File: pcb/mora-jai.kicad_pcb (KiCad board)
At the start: 2 copper layers, 150 x 150 mm, 74 parts, among them J1 Conn_01x02, J2 Conn_01x04, J3 Conn_01x02, J4 Conn_01x01, J5 Conn_01x03, SW1 SW_Push, SW10 SW_Push, SW11 SW_Push, SW12 SW_Push, SW13 SW_Push, SW14 SW_Push, SW15 SW_Push, SW16 SW_Push, SW2 SW_Push, SW3 SW_Push, SW4 SW_Push, SW5 SW_Push, SW6 SW_Push, SW7 SW_Push, SW8 SW_Push, SW9 SW_Push, U1 CD74HC4067M, U3 XIAO-ESP32-S3-SMD

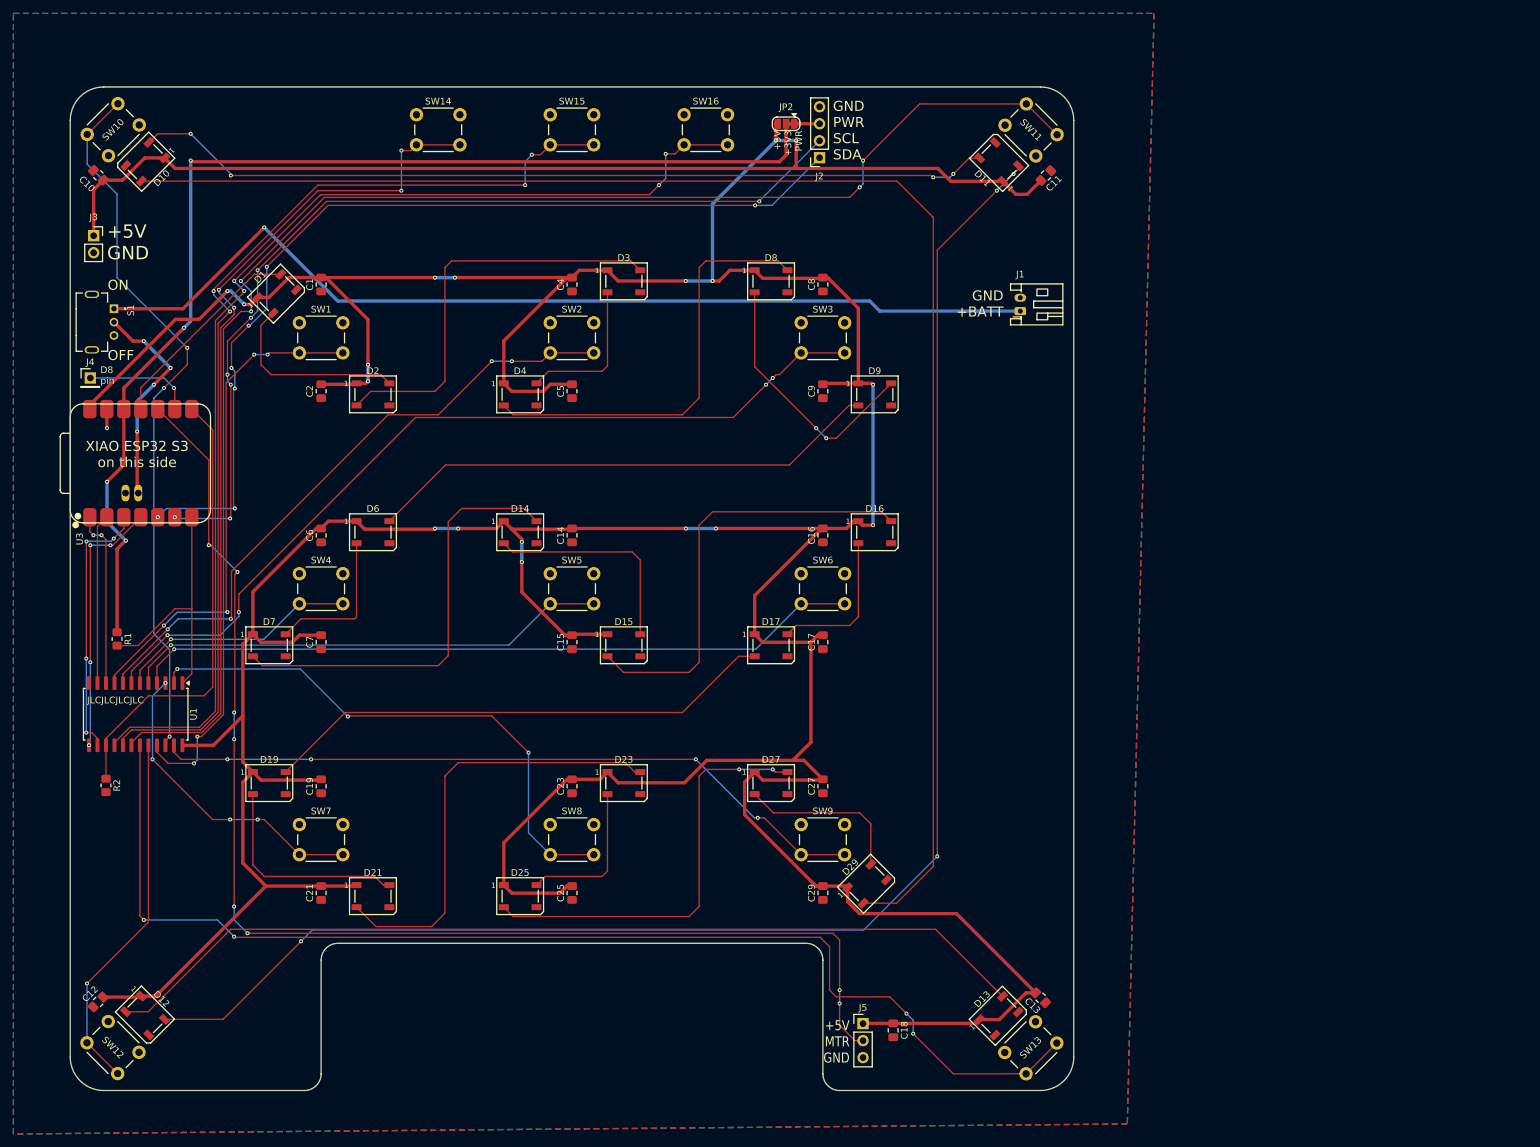
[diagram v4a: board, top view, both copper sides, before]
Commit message: add ground connecting vias
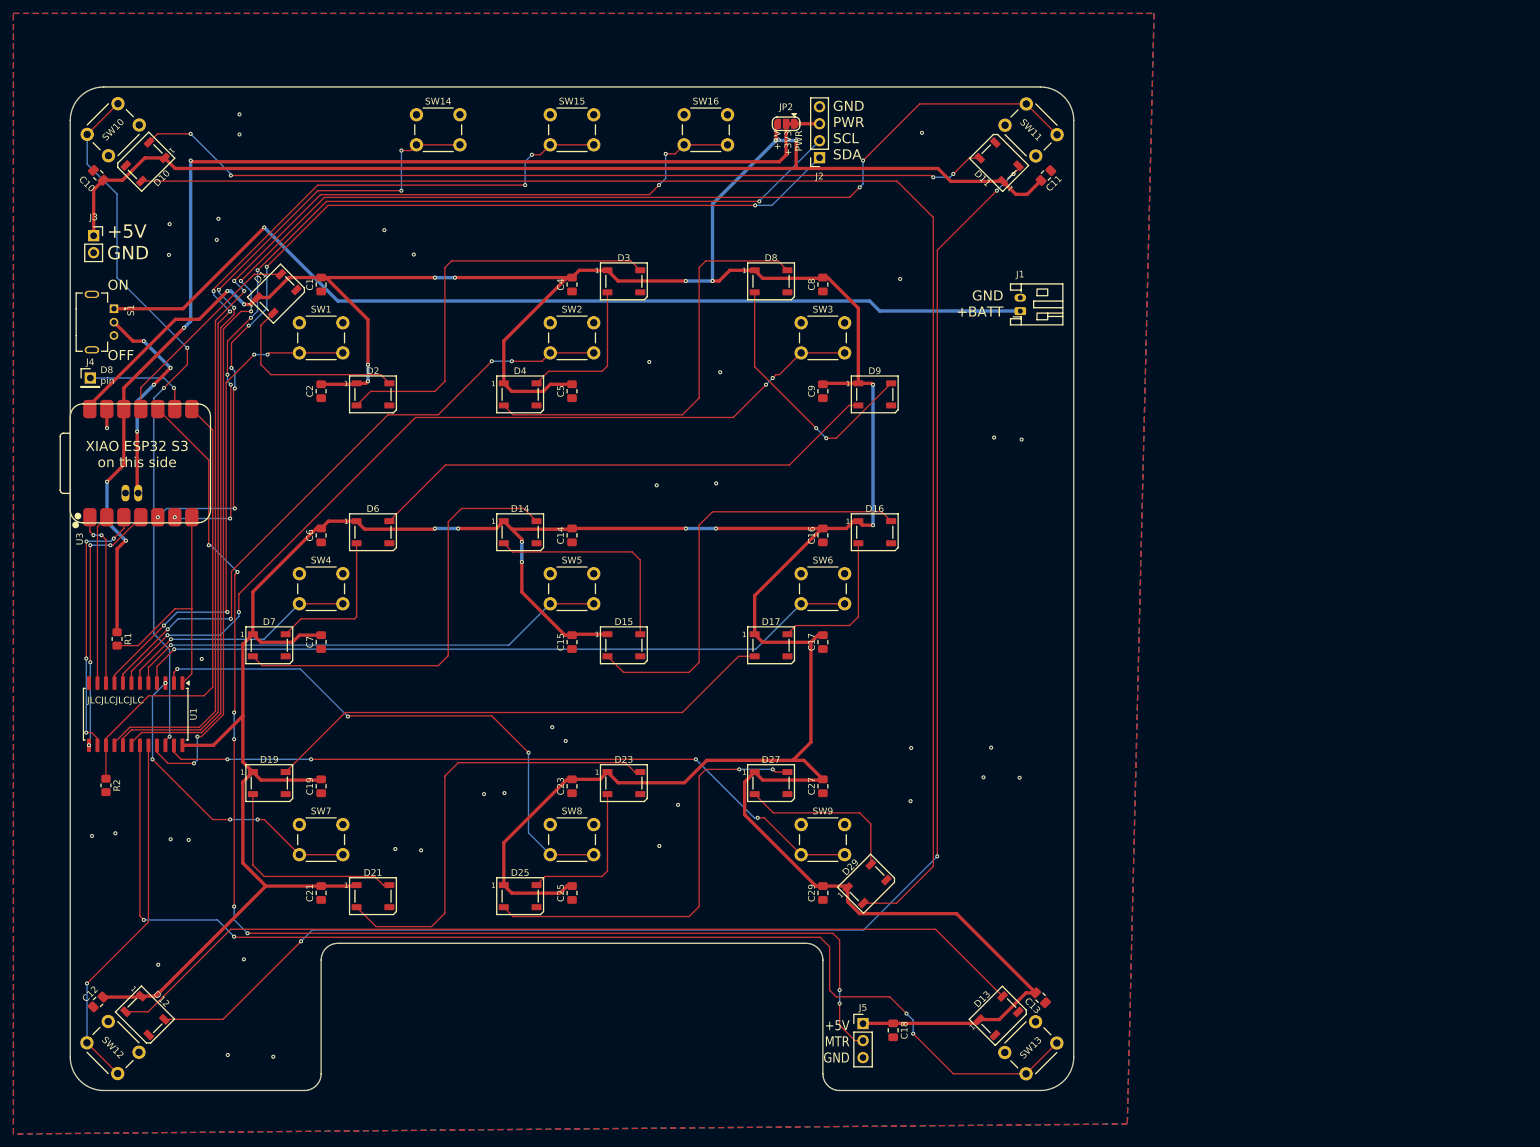
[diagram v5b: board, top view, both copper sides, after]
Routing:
- net GND: vias 1 -> 39

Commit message: add notes to PCB and schematic for revision 2
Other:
- board text added: "TODO: - Add mounting hole cutouts - Add battery charger & boost circuits (see schematic)"

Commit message: added mounting holes, 3.5mm diameter
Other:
- outline, holes or cut-outs redrawn
- board text added: "TODO: - Add battery charger & boost circuits (see schematic)"
- board text removed: "TODO: - Add mounting hole cutouts - Add battery charger & boost circuits (see schematic)"

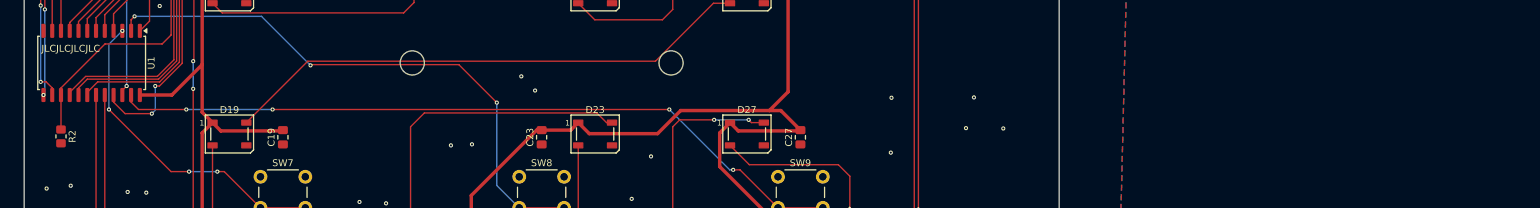
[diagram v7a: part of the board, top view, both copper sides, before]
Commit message: finished (?) schematic for rev. 2 power circuits
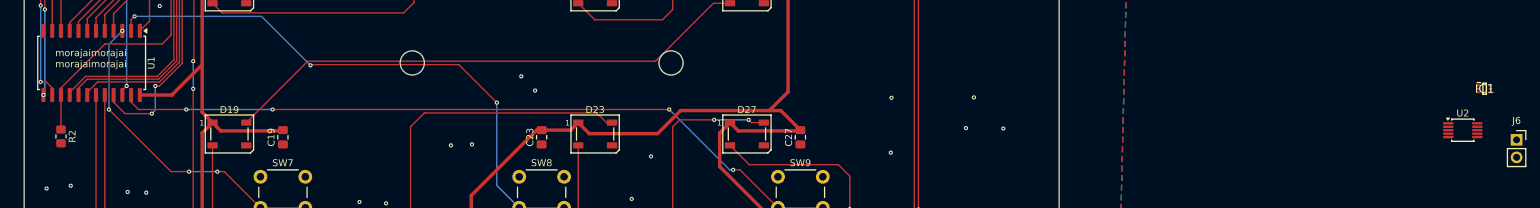
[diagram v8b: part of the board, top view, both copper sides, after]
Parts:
- added IC1: TPS61023DRLR, Mora_Jai_Parts:SOTFL50P160X60-6N, F.Cu at (237.7, 120.5)
- added J6: Conn_01x02, Connector_PinSocket_2.54mm:PinSocket_1x02_P2.54mm_Vertical, F.Cu at (242.3, 127.9)
- added U2: MCP73833-AMI-UN, Package_SO:MSOP-10_3x3mm_P0.5mm, F.Cu at (234.5, 126.5)
- R1, R2: value R -> 100kΩ
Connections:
- J1 pad 1: Net-(J1-Pin_1) -> unconnected-(J1-Pin_1-Pad1)
- R2 pad 1: /MUX_EN -> Net-(U1-~{E})
- S1 pad 1: Net-(J1-Pin_1) -> unconnected-(S1-Pad1)
- S1 pad 2: +BATT -> unconnected-(S1-Pad2)
- U1 pad 15: /MUX_EN -> Net-(U1-~{E})
- U3 pad 8: /MUX_EN -> ~{STAT1}
- U3 pad 9: D8_PIN -> BATT_V
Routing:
- net (no net): track 0.00 -> 213.7 mm, vias 0 -> 1
- net Net-(J1-Pin_1): track 145.7 -> 0.00 mm, vias 1 -> 0
- net /MUX_EN: track 68.0 -> 0.00 mm
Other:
- board text added: "morajaimorajai morajaimorajai"
- board text removed: "JLCJLCJLCJLC"
